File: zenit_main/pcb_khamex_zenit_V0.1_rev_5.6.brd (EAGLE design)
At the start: 146.7 x 215.3 mm, 47 parts, among them IC1 PCA9306JKZ, IC2 SN65HVD230DR, J1 612010235121, J2 52559-2253, J3 686110188622, J4 686110188622, U1 AMS1117-1.8

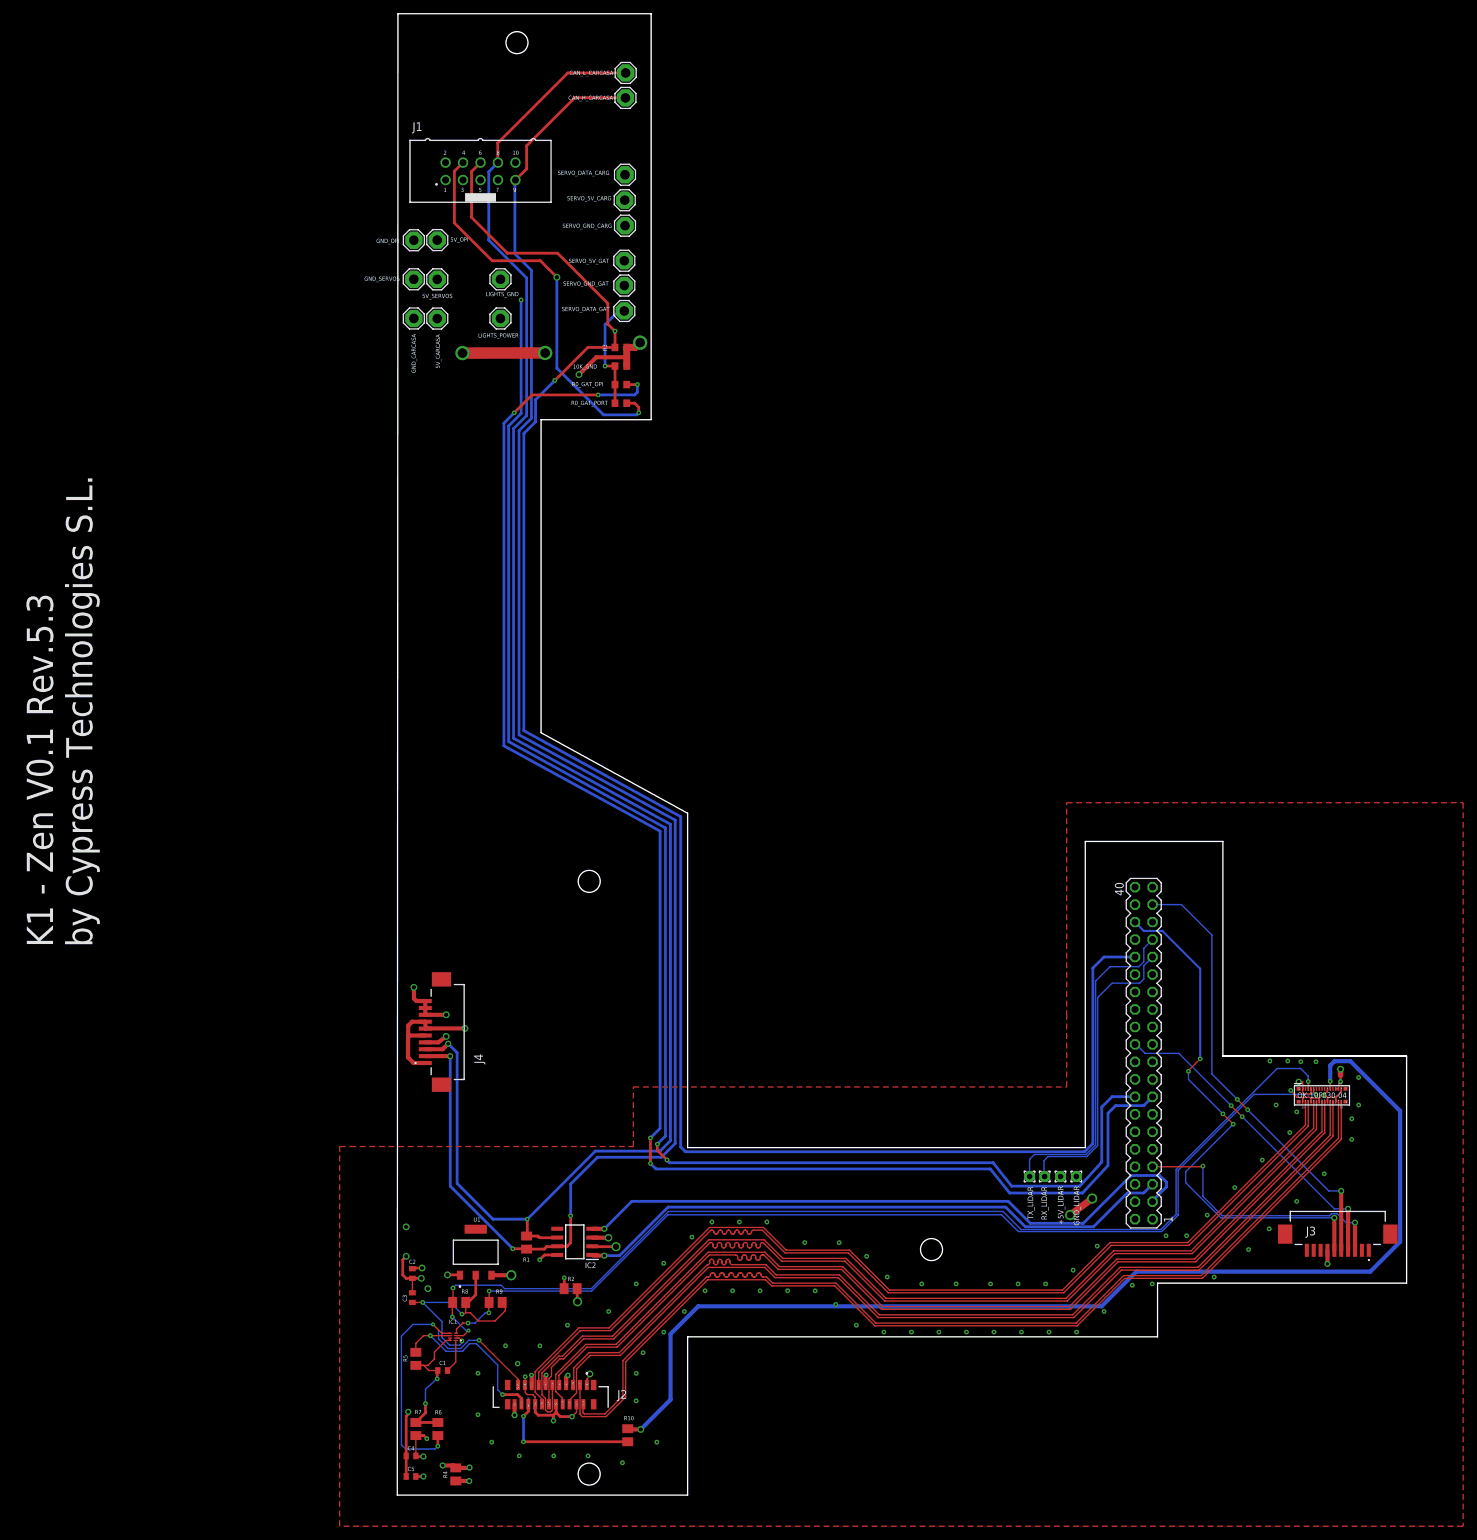
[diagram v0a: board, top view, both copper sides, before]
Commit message: JC: Cambios en zenit y rotor
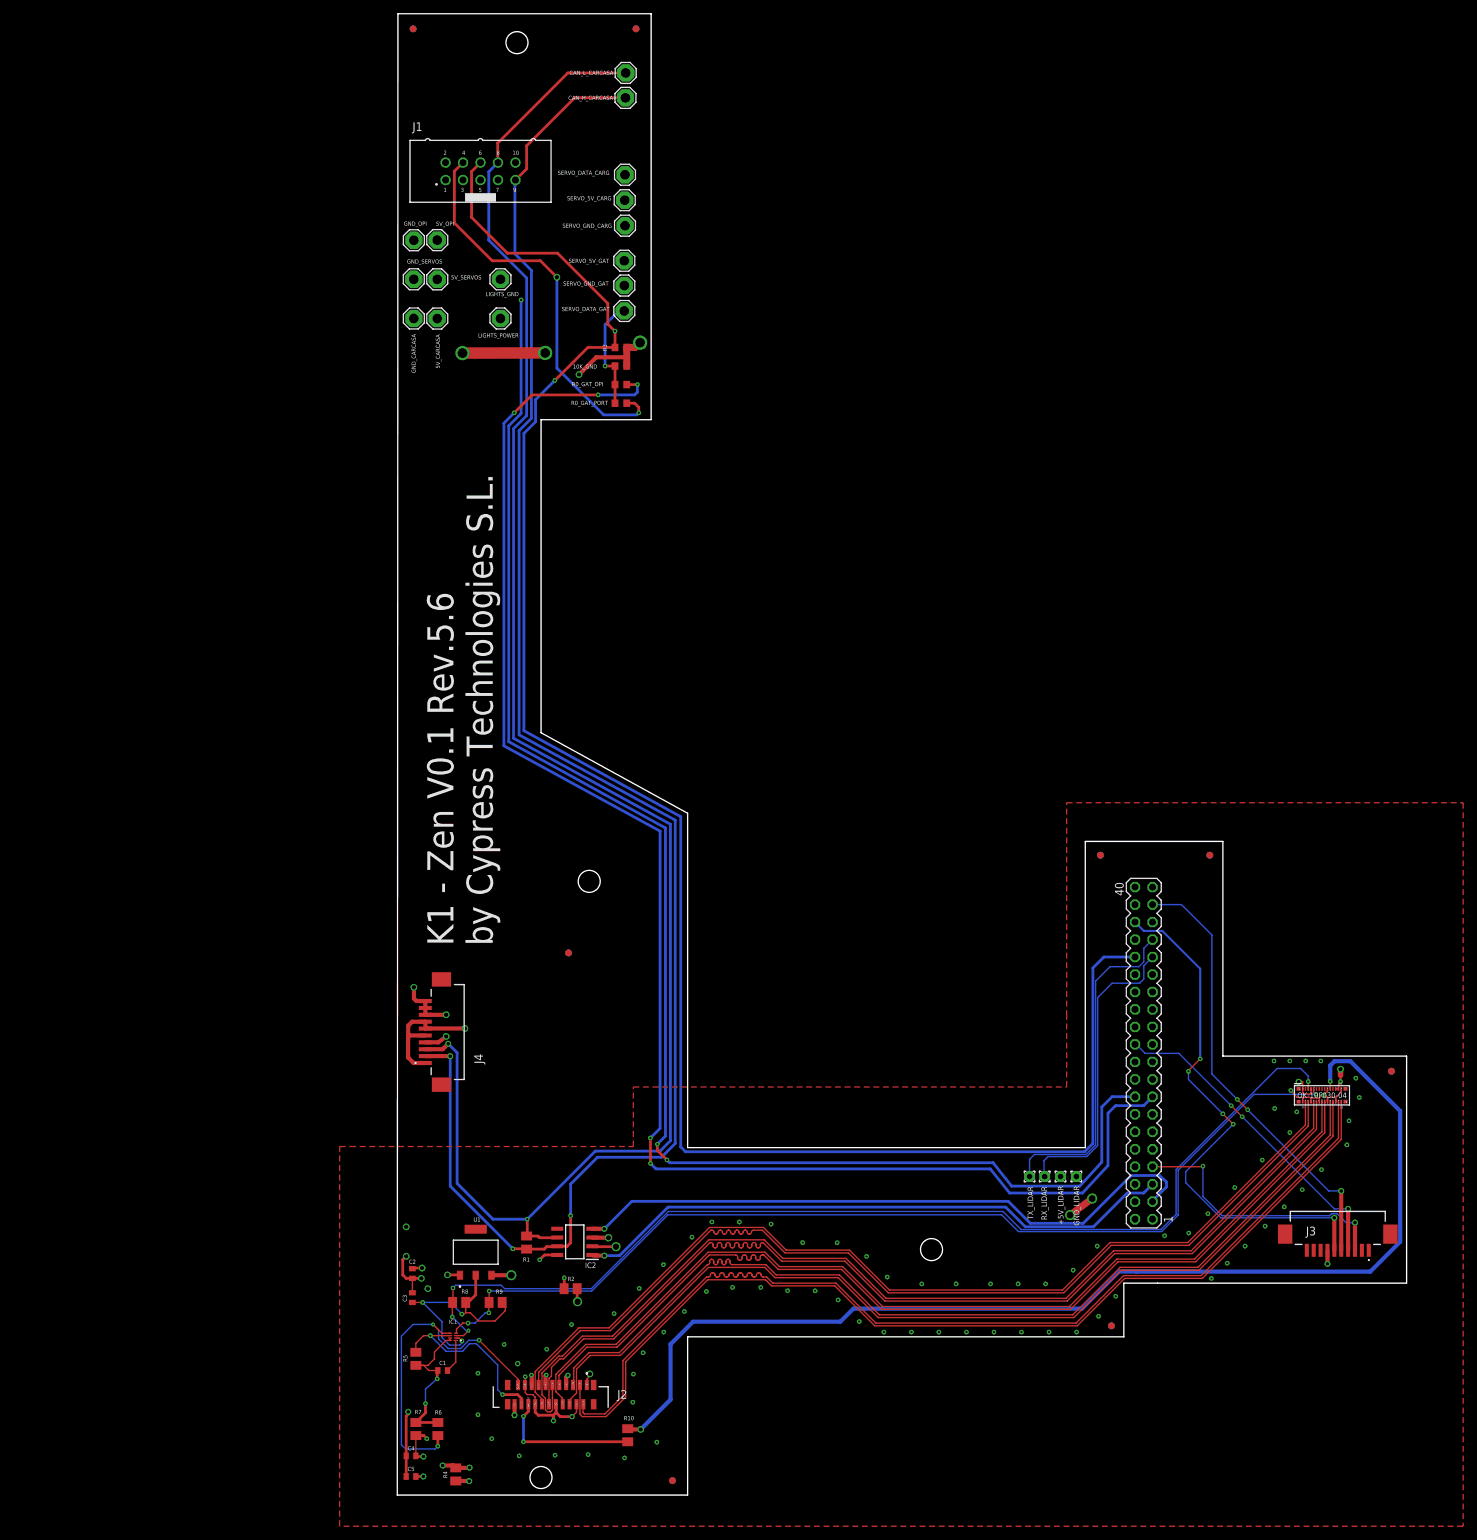
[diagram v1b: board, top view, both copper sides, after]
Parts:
- added U$2, U$3, U$4, U$5, U$6, U$7, U$8, U$9: (no value), fiducial:CIRCLE-1MM-3R
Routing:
- net CLK: track 165.1 -> 164.3 mm
- net GND_OPI: vias 93 -> 94
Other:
- outline, holes or cut-outs redrawn
- board text added: "K1 - Zen V0.1 Rev.5.6 by Cypress Technologies S.L."
- board text removed: "K1 - Zen V0.1 Rev.5.3 by Cypress Technologies S.L."
